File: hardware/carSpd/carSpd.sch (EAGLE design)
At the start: 66 parts, among them IC1 MCP16301/H, IC2 CP2102, IC3 DS3231/SO, Q1 2n3904, U1 ATMEGA328P_TQFP, U3 ERC1602-4SMD-LED, U4 DS1820, Y1 16mhz, Y2 16MHZ

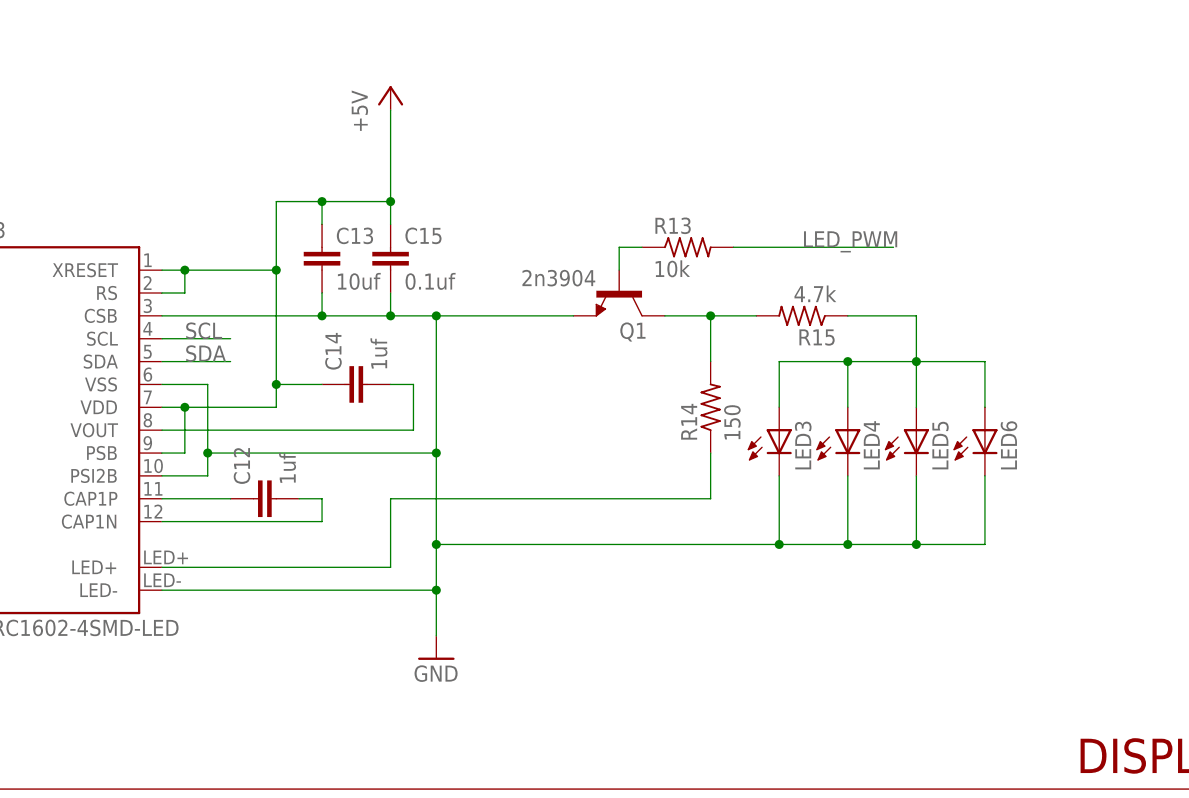
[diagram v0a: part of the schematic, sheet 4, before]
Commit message: Corrected and verified schematics
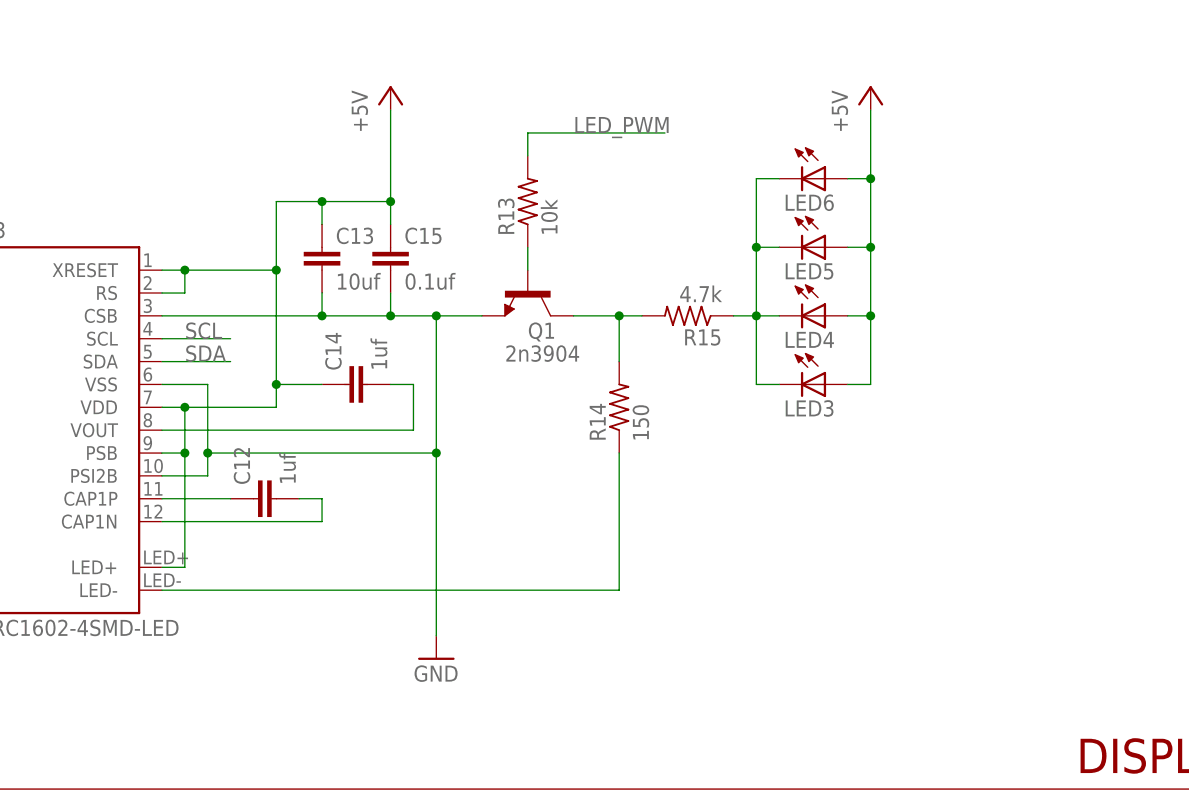
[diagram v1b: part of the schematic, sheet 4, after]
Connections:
- removed net N$23: LED3.A, LED4.A, LED5.A, LED6.A, R15.1
- removed net N$25: C7.2, IC1.VFB, R8.1, R9.1
- new net N$1: IC1.VFB, R8.1, R9.1
- new net N$2: LED3.C, LED4.C, LED5.C, LED6.C, R15.1
- net +5V: now also LED3.A, LED4.A, LED5.A, LED6.A, U3.LED+
- net GND: now also C7.2; no longer LED3.C, LED4.C, LED5.C, LED6.C, U3.LED-
- net N$16: now also U3.LED-; no longer U3.LED+
- net TEMP: now also U1.PB2(SS/OC1B)
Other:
- note added: "MCP16301"
- moved on the sheet: LED3, LED4, LED5, LED6, Q1, R13, R14, R15, R8

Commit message: Routing complete
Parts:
- added H1, H2, H3, H4: STAND-OFF, SparkFun-Hardware:STAND-OFF
- C6: value 100nf -> 0.1uf
- L1: device rcl:L-USL3225M -> hybridair:CBC2518T220M
- SV1: device con-lsta:FE06W -> con-lsta:FE05W
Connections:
- removed net N$28: S2.1, U1.PD6(AIN0)
- removed net N$29: LED2.A, R12.1
- removed net N$33: S3.1, U1.PB0(ICP)
- removed net N$34: S4.1, U1.PD7(AIN1)
- removed net N$35: S5.1, U1.PB1(OC1A)
- new net N$13: S5.1, U1.PD4(XCK/T0)
- new net N$3: LED2.C, R12.1
- new net N$5: S2.1, U1.PC1(ADC1)
- new net N$6: S4.1, U1.PC2(ADC2)
- new net N$7: S3.1, U1.PC3(ADC3)
- net +12V: now also SV1.1; no longer SV1.2
- net +5V: now also LED2.A; no longer R12.2, SV1.1
- net GND: now also R12.2, SV1.5; no longer LED2.C, SV1.6
- net INJ: now also SV1.3; no longer SV1.4
- net LIGHTING: now also SV1.4; no longer SV1.5
- net VSS: now also SV1.2; no longer SV1.3
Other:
- moved on the sheet: LED2, R12, S2, S3, S4, S5

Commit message: PCB design complete
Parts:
- added LED7, LED8: (no value), led:LEDCHIPLED_0805
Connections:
- net +5V: now also LED7.A, LED8.A
- net N$2: now also LED7.C, LED8.C
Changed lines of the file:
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@@
 <part name="H4" library="SparkFun-Hardware" deviceset="STAND-OFF" device=""/>
 <part name="SV1" library="con-lsta" deviceset="FE05W" device="" value="CAR_INPUT"/>
+<part name="LED7" library="led" deviceset="LED" device="CHIPLED_0805"/>
+<part name="LED8" library="led" deviceset="LED" device="CHIPLED_0805"/>
 </parts>
 <sheets>
@@
 <instance part="R12" gate="G$1" x="55.88" y="45.72"/>
 <instance part="P+16" gate="1" x="114.3" y="167.64"/>
+<instance part="LED7" gate="G$1" x="109.22" y="127" rot="R270"/>
+<instance part="LED8" gate="G$1" x="109.22" y="119.38" rot="R270"/>
 </instances>
 <busses>
@@
 <junction x="114.3" y="157.48"/>
 <pinref part="P+16" gate="1" pin="+5V"/>
+<pinref part="LED8" gate="G$1" pin="A"/>
+<wire x1="111.76" y1="119.38" x2="114.3" y2="119.38" width="0.1524" layer="91"/>
+<wire x1="114.3" y1="119.38" x2="114.3" y2="127" width="0.1524" layer="91"/>
+<pinref part="LED7" gate="G$1" pin="A"/>
+<wire x1="114.3" y1="127" x2="111.76" y2="127" width="0.1524" layer="91"/>
+<wire x1="114.3" y1="127" x2="114.3" y2="134.62" width="0.1524" layer="91"/>
+<junction x="114.3" y="127"/>
+<junction x="114.3" y="134.62"/>
 </segment>
 </net>
@@
 <pinref part="LED6" gate="G$1" pin="C"/>
 <wire x1="101.6" y1="157.48" x2="104.14" y2="157.48" width="0.1524" layer="91"/>
-</segment>
-</net>
+<wire x1="101.6" y1="134.62" x2="101.6" y2="127" width="0.1524" layer="91"/>
+<junction x="101.6" y="134.62"/>
+<pinref part="LED7" gate="G$1" pin="C"/>
+<wire x1="101.6" y1="127" x2="104.14" y2="127" width="0.1524" layer="91"/>
+<wire x1="101.6" y1="127" x2="101.6" y2="119.38" width="0.1524" layer="91"/>
+<junction x="101.6" y="127"/>
+<pinref part="LED8" gate="G$1" pin="C"/>
+<wire x1="104.14" y1="119.38" x2="101.6" y2="119.38" width="0.1524" layer="91"/>
+</segment>
+</net>
